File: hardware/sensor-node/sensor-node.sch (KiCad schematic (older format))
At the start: 51 parts, among them J1 CONUFL001-SMD-T, J2 SHF-105-01-L-D-TH, Q1 PMV250EPEA, U1 TLV61225, U2 TPS27081A, U3 SHT31-DIS, U4 24LC32, U5 MLX90614, U6 ADG633YRU, U7 TSV911RILT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

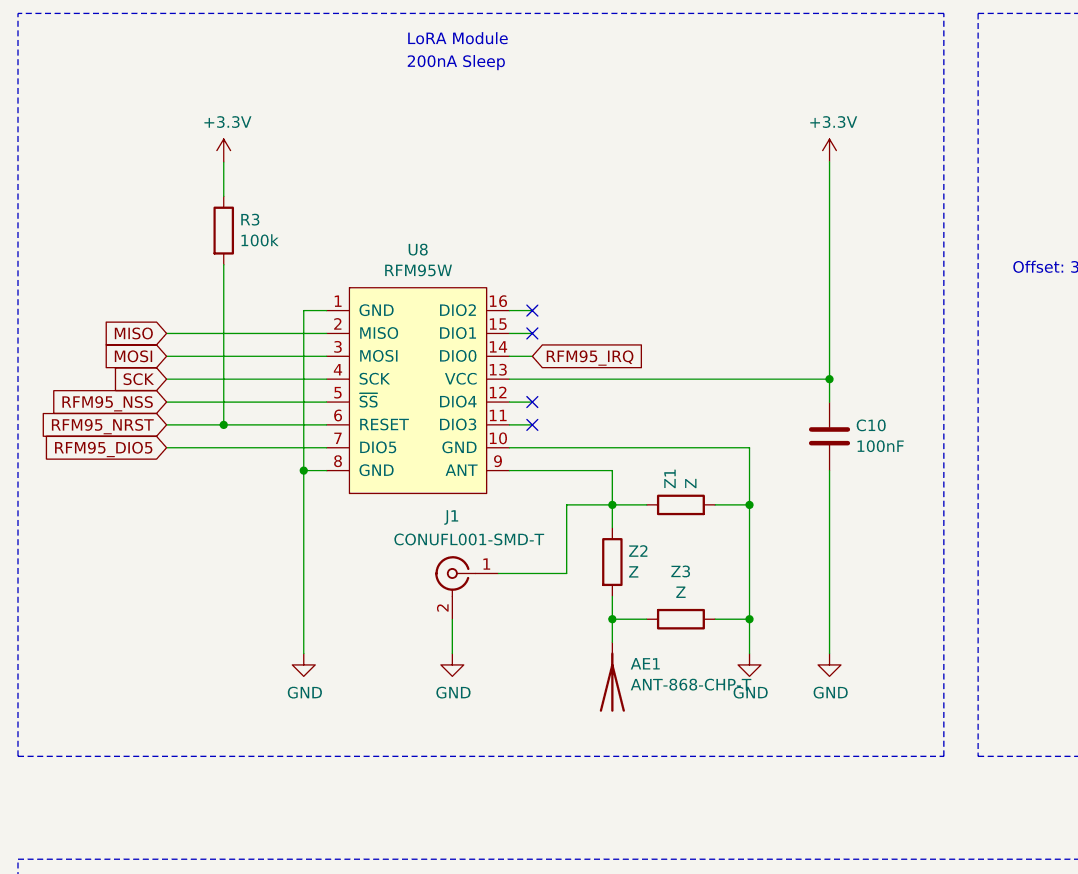
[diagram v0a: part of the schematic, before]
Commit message: Seperate local dev and test deployments, fix TTN device ID generation
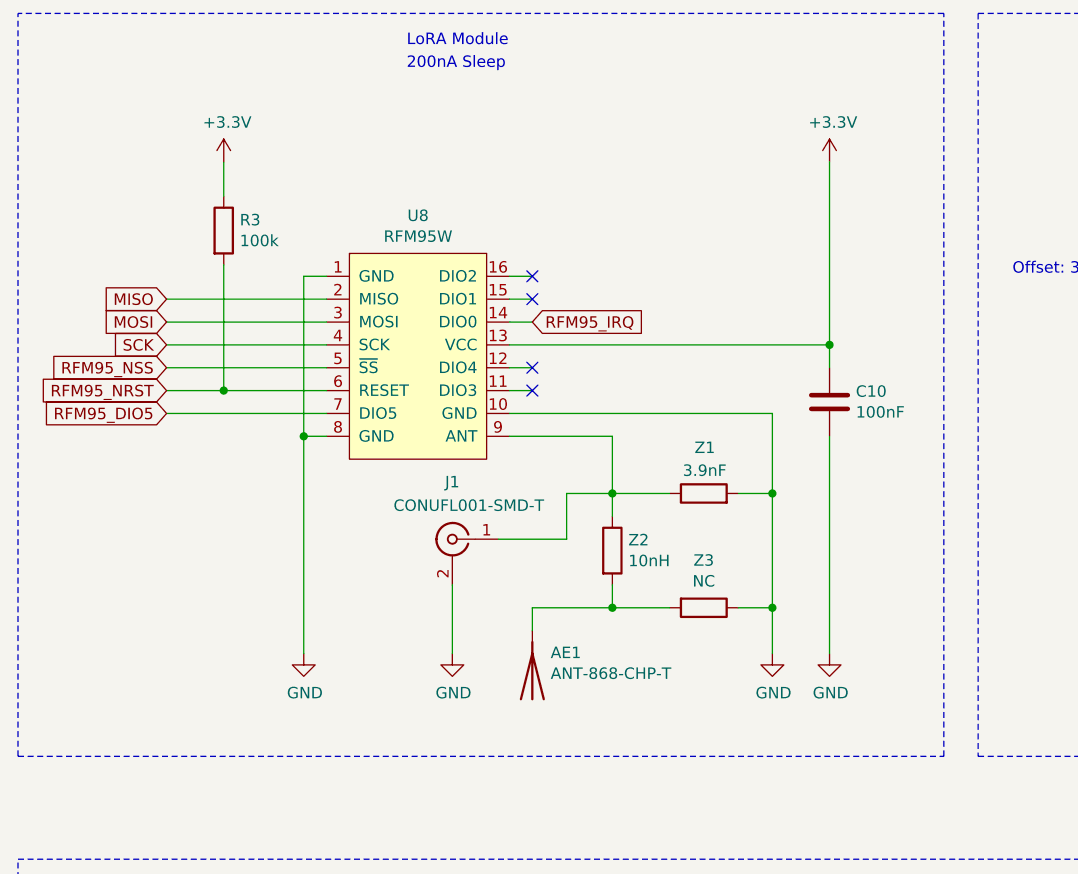
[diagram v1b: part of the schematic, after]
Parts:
- Z1: value Z -> 3.9nF
- Z2: value Z -> 10nH
- Z3: value Z -> NC
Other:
- moved on the sheet: AE1, C10, J1, U8, Z1, Z2, Z3
